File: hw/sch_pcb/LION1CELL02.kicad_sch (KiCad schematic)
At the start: 90 parts, among them J1 USBC_USB4105-GF-A, J2 HEADER_2x03, J3 HEADER_1x04, Q1 BSS83P, Q2 BC807-25, Q3 BC807-25, Q4 SI2302A-TP, Q5 SI2302A-TP, SW1 SKRTLAE010, U1 BQ34Z100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

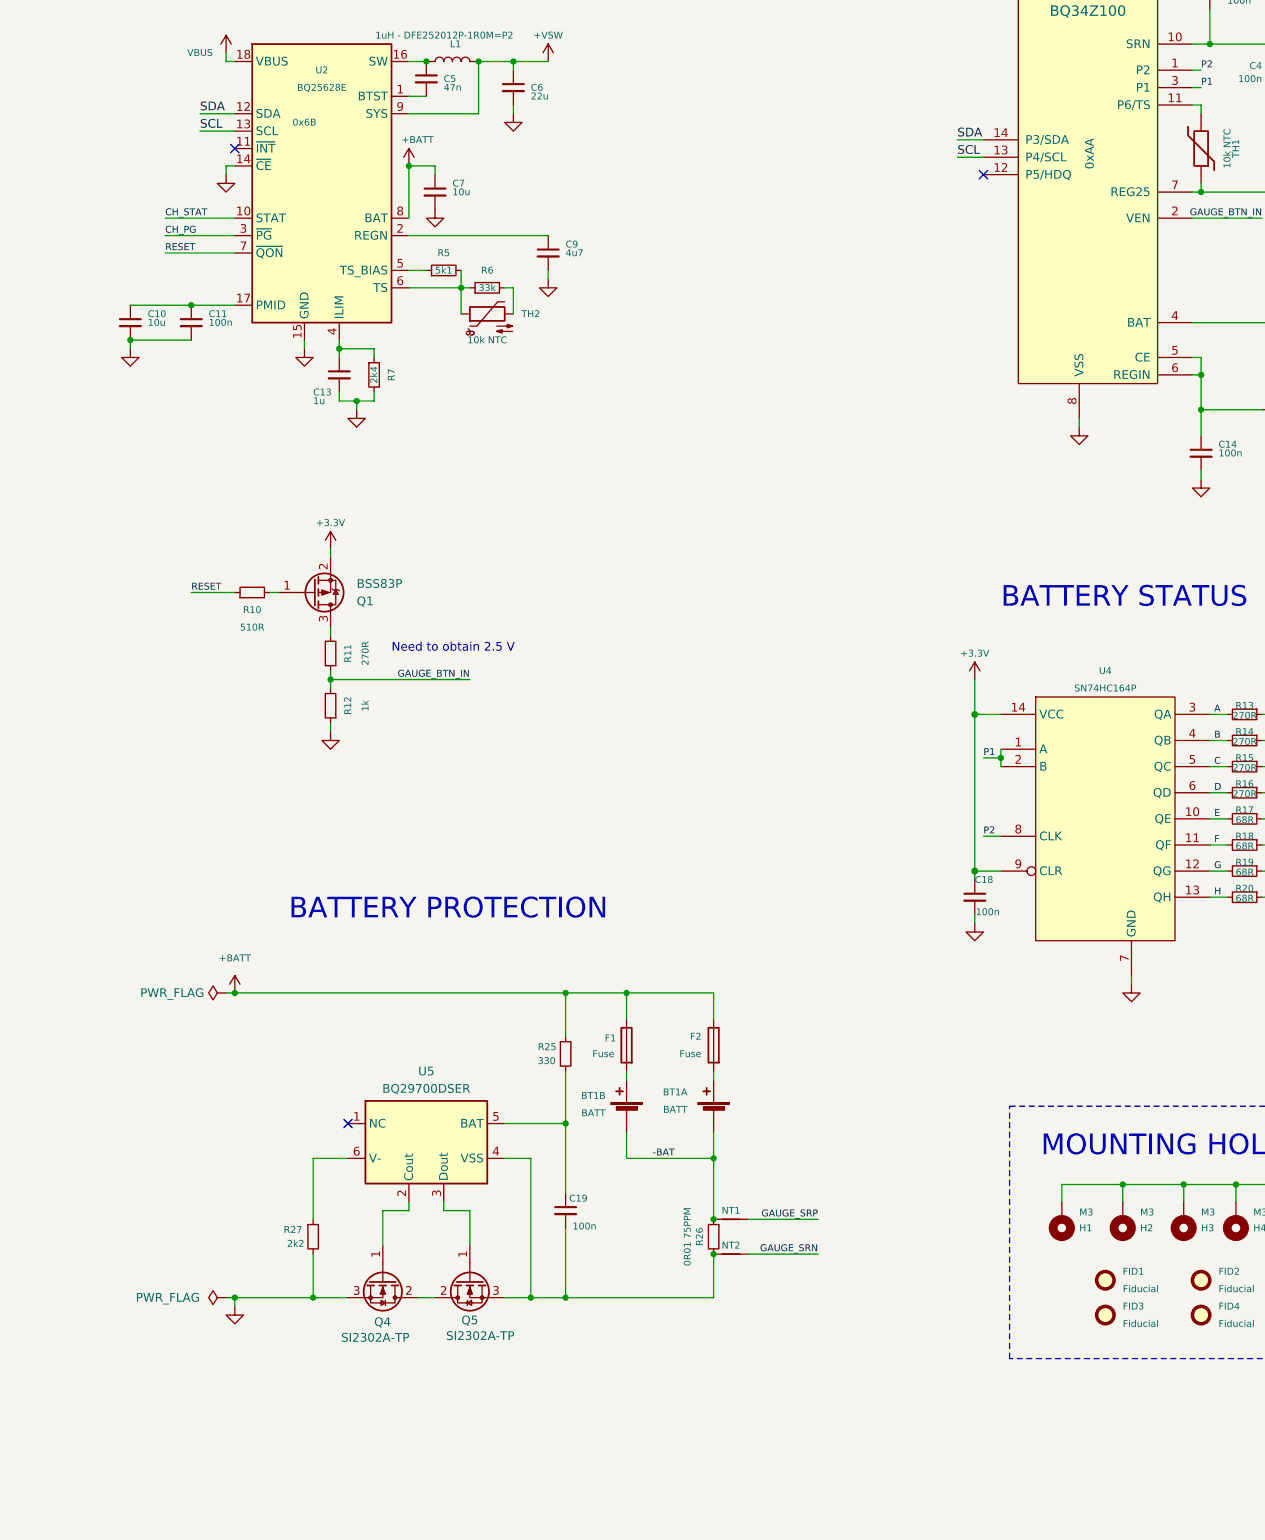
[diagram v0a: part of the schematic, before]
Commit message: Pridani ochrany proti prehrati pres alert pin
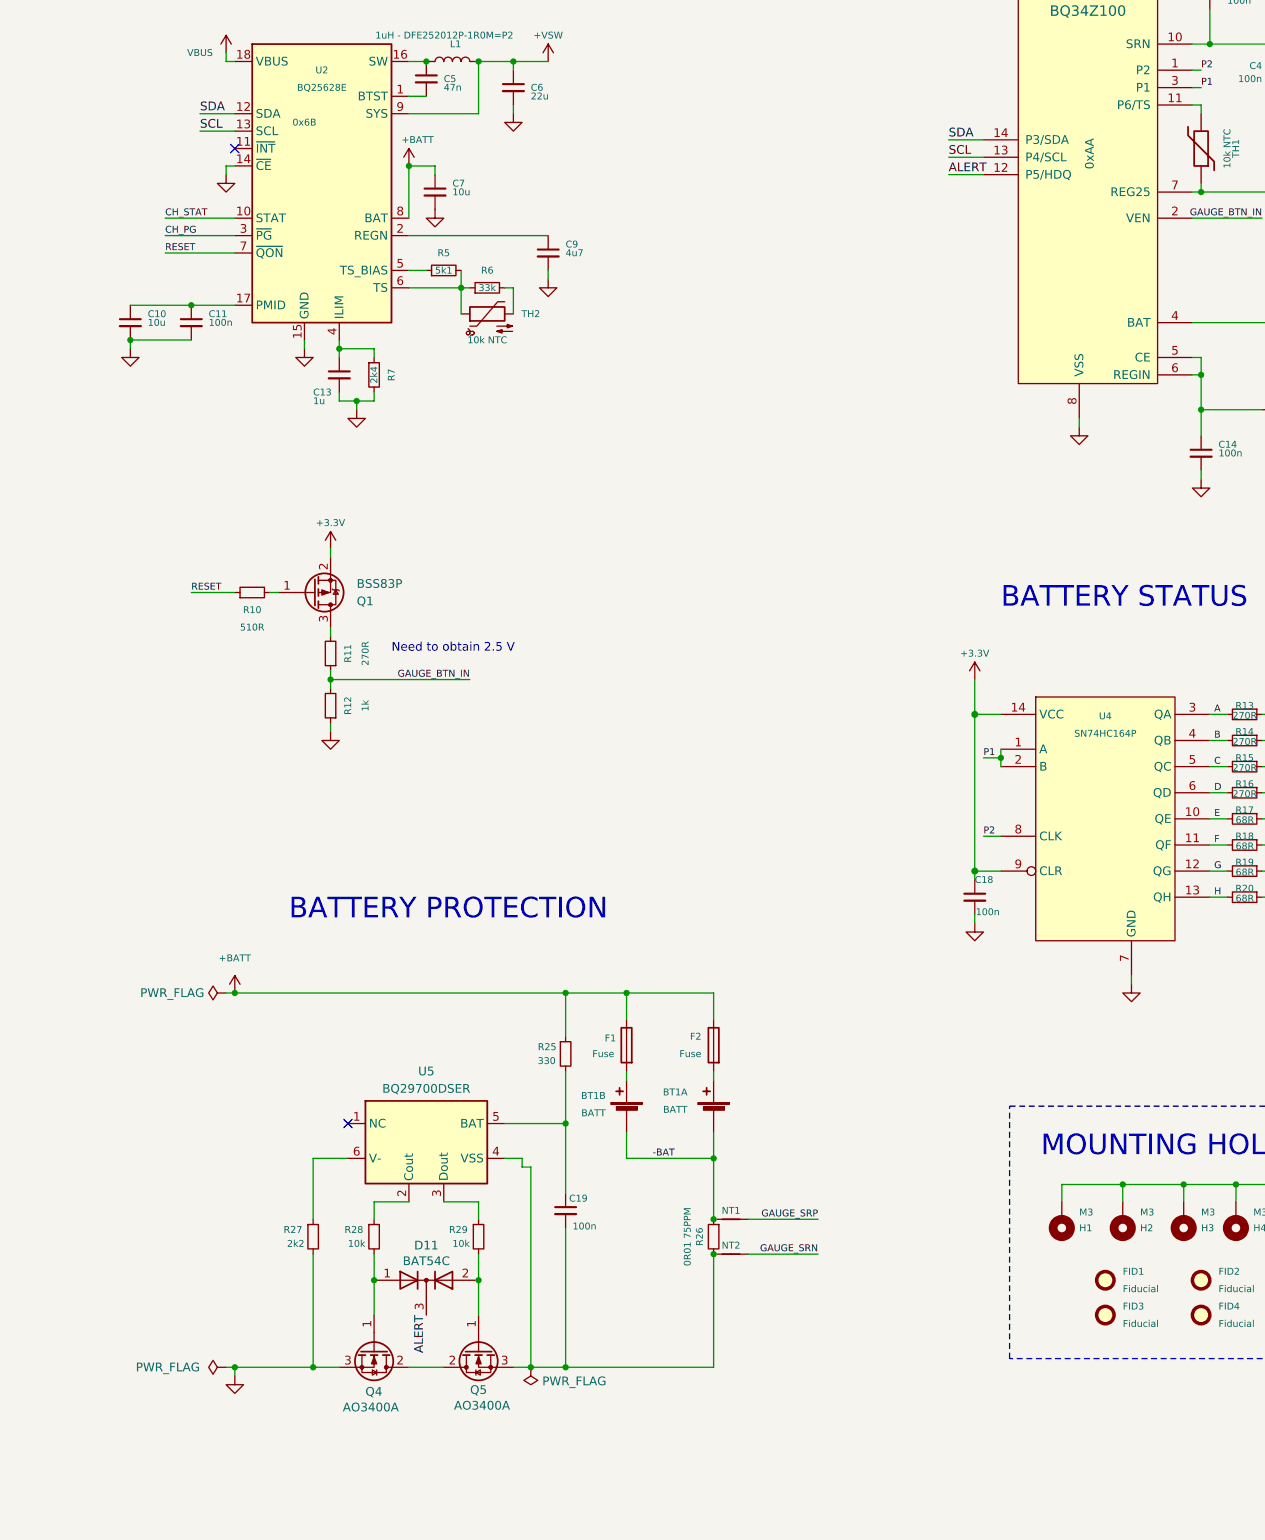
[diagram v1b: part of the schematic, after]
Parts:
- added D11: BAT54C, Mlab_IO:SOT-23, symbol Device:D_Dual_CommonCathode_AAK
- added R28, R29: 10k, Resistor_SMD:R_0805_2012Metric, symbol Device:R_Small
- Q4, Q5: value SI2302A-TP -> AO3400A
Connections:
- net at Q5.1 (G): now also D11.2 (A), R29.2; no longer U5.3 (Dout)
- net ALERT: now reaches U1.12 (P5/HDQ)
- net ALERT: now also D11.3 (K)
- net at U5.2 (Cout): now also R28.1; no longer Q4.1 (G)
- new net: D11.1 (A), Q4.1 (G), R28.2
- new net: R29.1, U5.3 (Dout)
- no-connect marks 9 -> 8
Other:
- moved on the sheet: Q4, Q5

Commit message: Update sch
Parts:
- R28, R29: value 10k -> 1k
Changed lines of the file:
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@@
 			)
 		)
-		(property "Value" "10k"
-			(at 193.04 225.806 0)
+		(property "Value" "1k"
+			(at 193.548 225.806 0)
 			(effects
 				(font
@@
 			)
 		)
-		(property "Value" "10k"
-			(at 208.28 225.806 0)
+		(property "Value" "1k"
+			(at 208.788 225.806 0)
 			(effects
 				(font

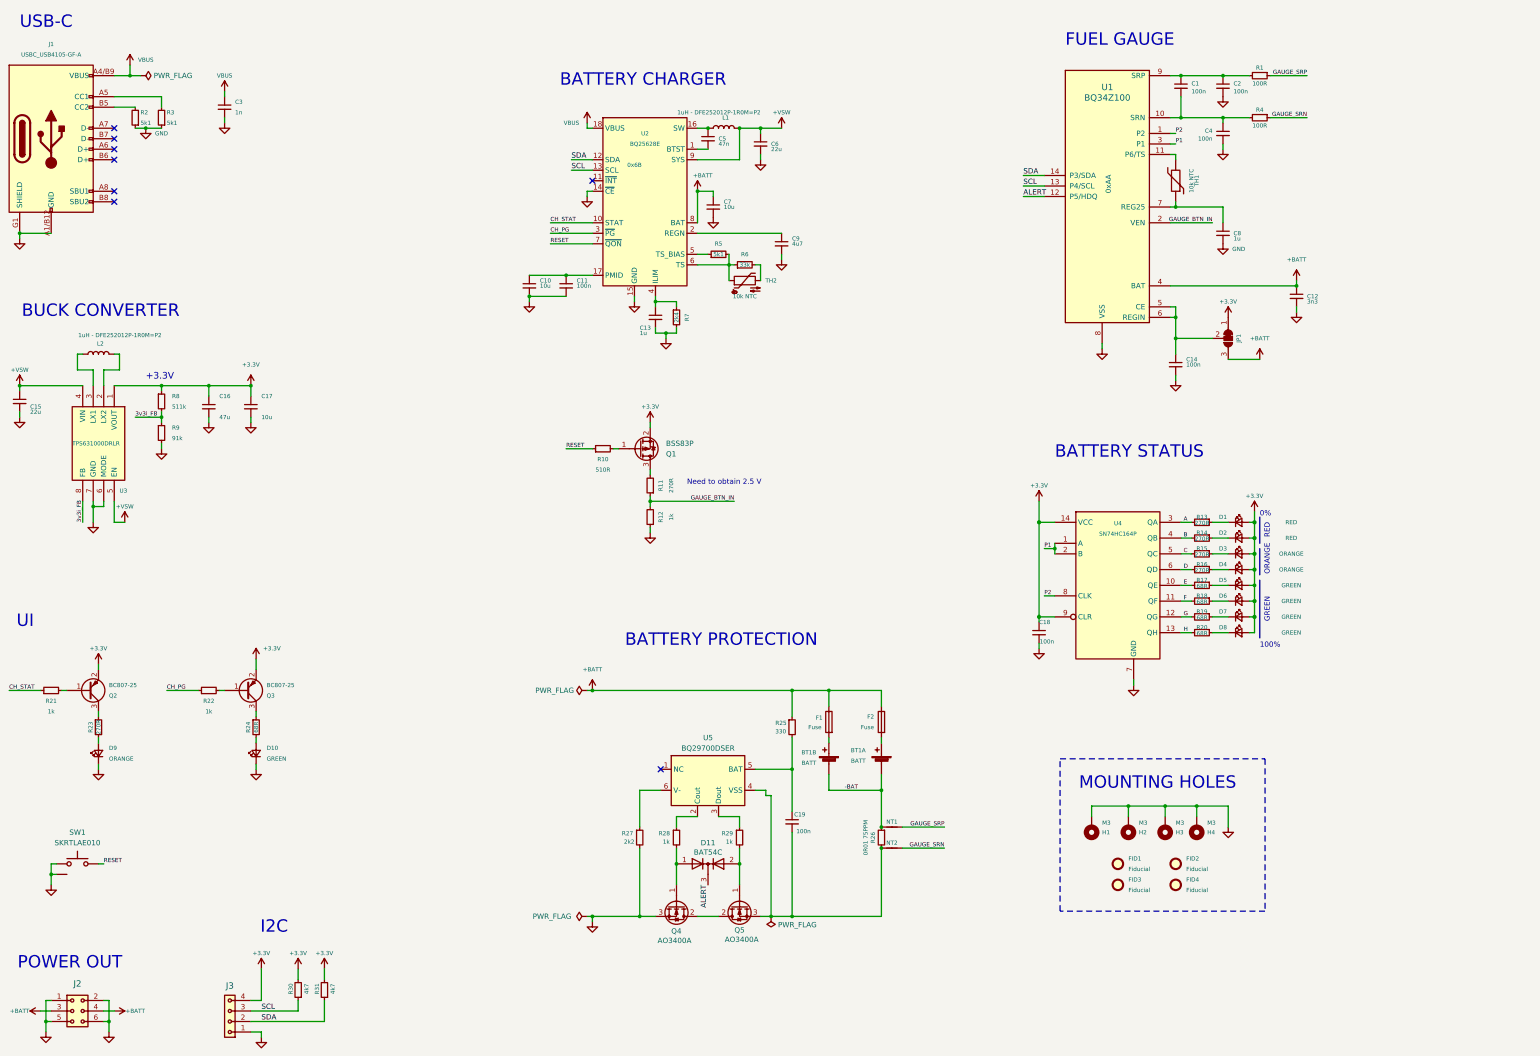
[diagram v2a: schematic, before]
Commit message: Move sensing resistor bellow protection transistors.
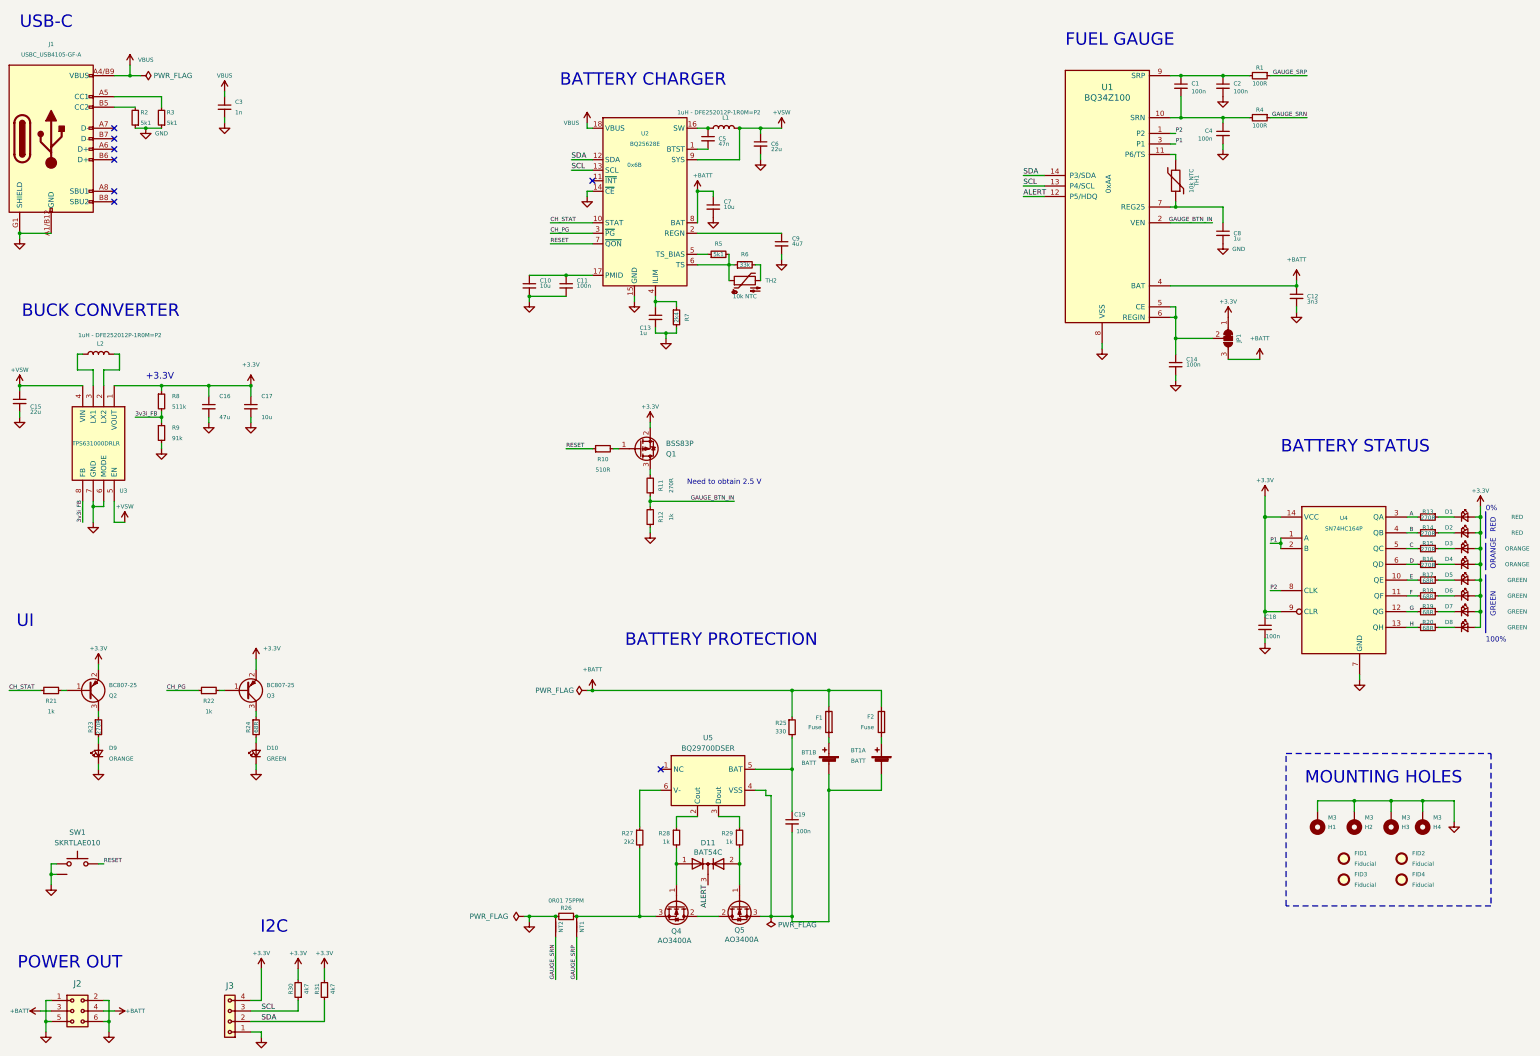
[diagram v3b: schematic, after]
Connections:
- net GND: now also NT2.2, R26.2; no longer Q4.3 (S), R27.2
- net at C19.2, Q5.3 (S), U5.4 (VSS): now also BT1.1- (-), BT1.2- (-); no longer NT2.2, R26.2
- net -BAT: no longer names the net of NT1.2, R26.1
- net -BAT: now also Q4.3 (S), R27.2; no longer BT1.1- (-), BT1.2- (-)
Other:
- moved on the sheet: C18, D1, D2, D3, D4, D5, D6, D7, D8, FID1, FID2, FID3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
